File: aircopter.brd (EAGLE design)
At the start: 47 x 28 mm, 44 parts, among them IC1 STF202-22T1G, M1 WIRELESS-NRF24L01, U2 GY-521MPU6050, Y1 20 MHz

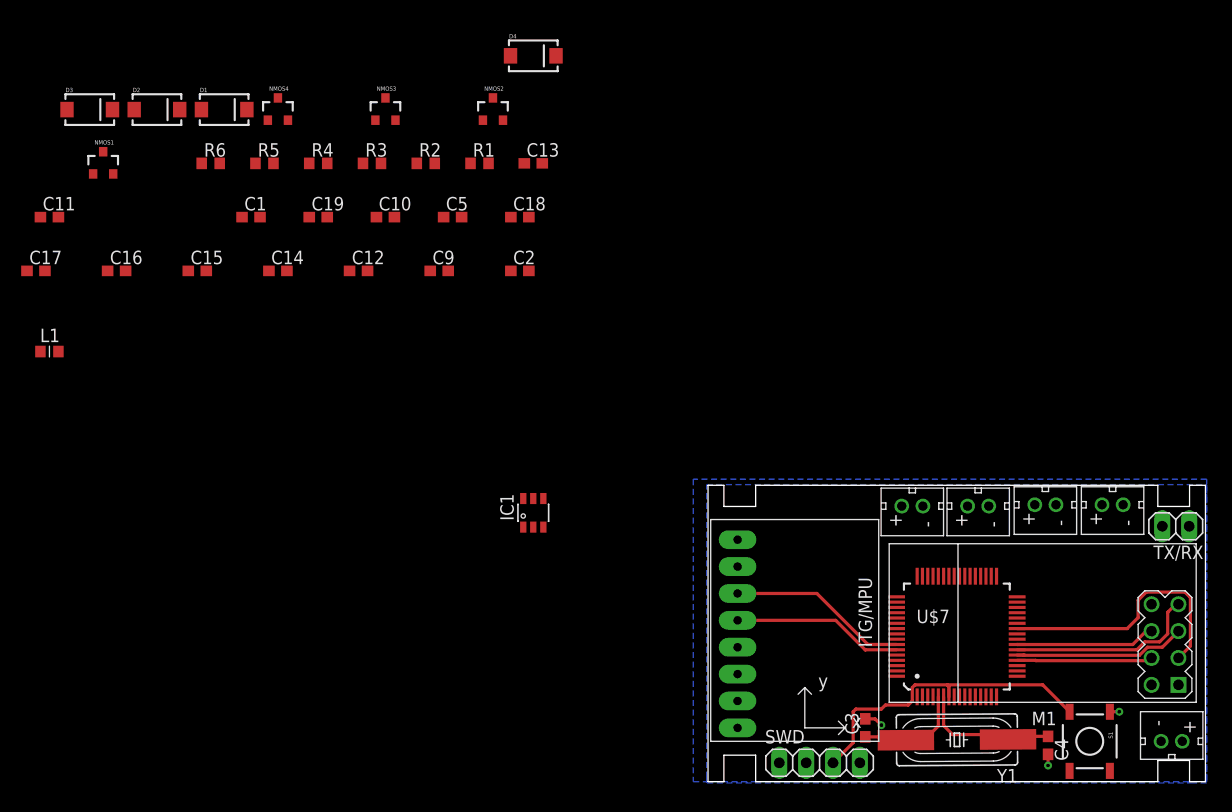
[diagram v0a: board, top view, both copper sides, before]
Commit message: Added Various Decoupling Caps
Can someone check them b4 merge with master pls
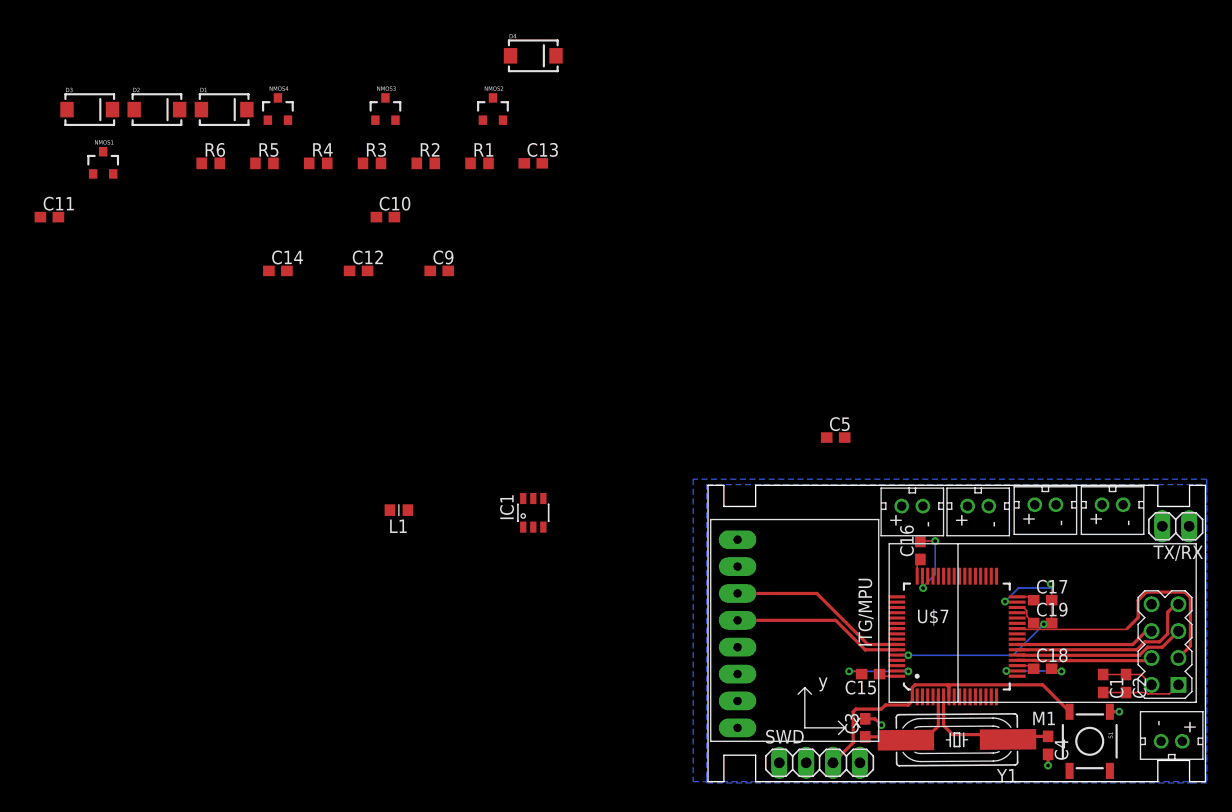
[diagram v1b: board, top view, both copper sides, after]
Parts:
- moved C17 100.1 mm to (31.6, 17.1)
- moved C1 91.8 mm to (37.3, 9.27), turned to 270 degrees
- moved C16 80.4 mm to (20.1, 21.8), turned to 90 degrees
- moved C19 78.5 mm to (31.6, 15.0)
- moved C15 74.2 mm to (15.4, 10.2), turned to 180 degrees
- moved C2 69.3 mm to (39.5, 9.27), turned to 270 degrees
- moved C18 65.3 mm to (31.6, 10.7)
- moved C5 41.8 mm to (12.1, 32.5)
- moved L1 36.3 mm to (-29.2, 25.7), turned to 180 degrees
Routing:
- net GND: track 3.71 -> 60.0 mm, vias 3 -> 13
- net 3V3: track 0.00 -> 11.7 mm
- net N$7: track 0.00 -> 2.47 mm
- net CE: track 25.2 -> 24.6 mm

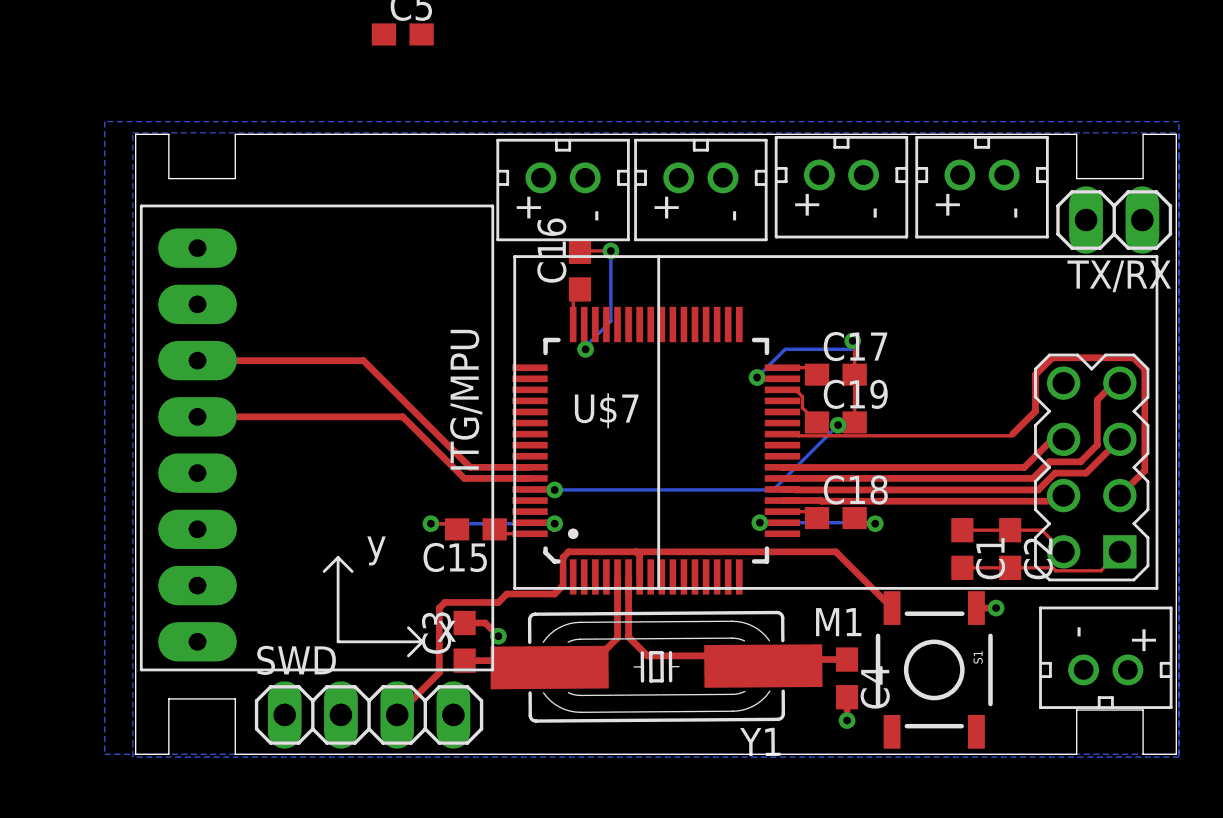
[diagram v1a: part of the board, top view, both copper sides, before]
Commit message: Fixed bugs, removed GND traces
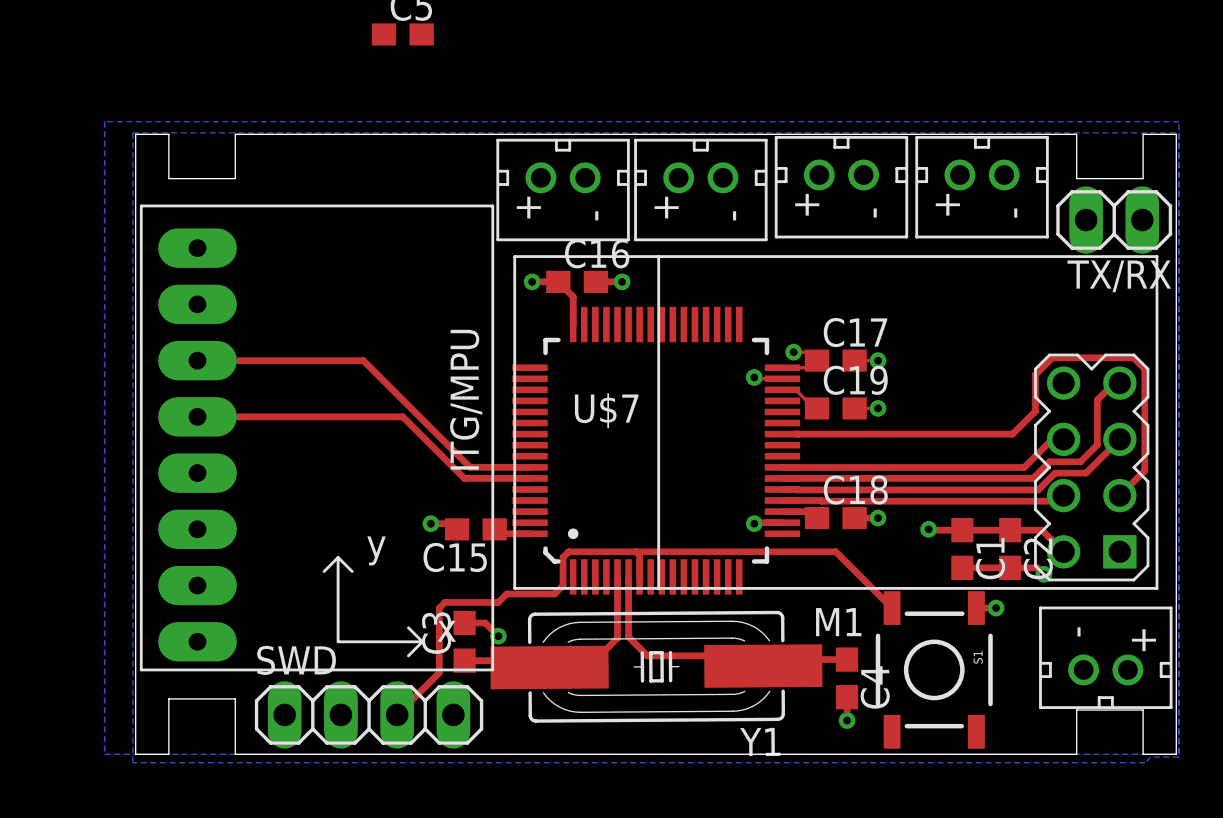
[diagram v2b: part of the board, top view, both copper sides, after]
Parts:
- moved C17 0.64 mm to (31.6, 17.8)
- moved C19 0.63 mm to (31.6, 15.6)
- moved C16 0.52 mm to (19.9, 21.3), turned to 0 degrees
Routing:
- net GND: track 60.0 -> 16.1 mm, vias 13 -> 11
- net 3V3: track 11.7 -> 16.2 mm, vias 0 -> 3
- net N$7: track 2.47 -> 1.91 mm

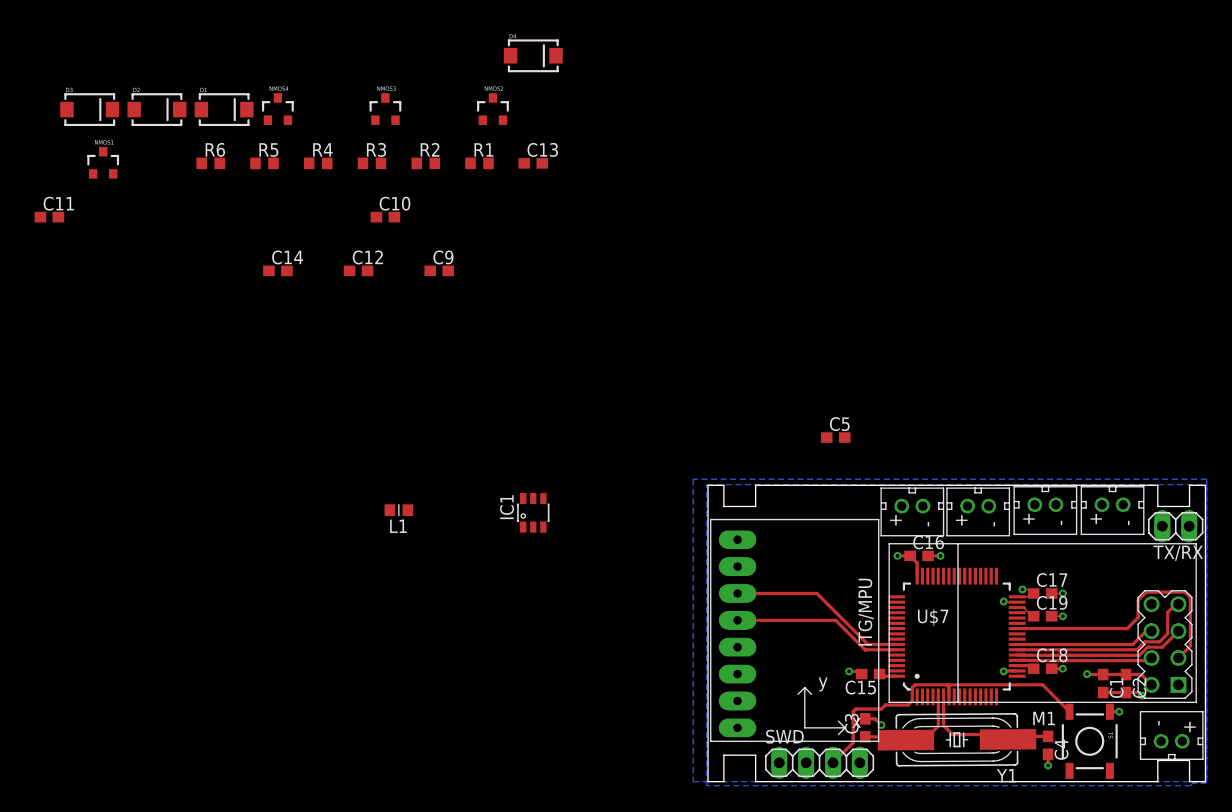
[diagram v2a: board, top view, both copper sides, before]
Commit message: Added remaining caps, organized remaining components
We're still missing the voltage regulator, voltage divider, and motor drivers,
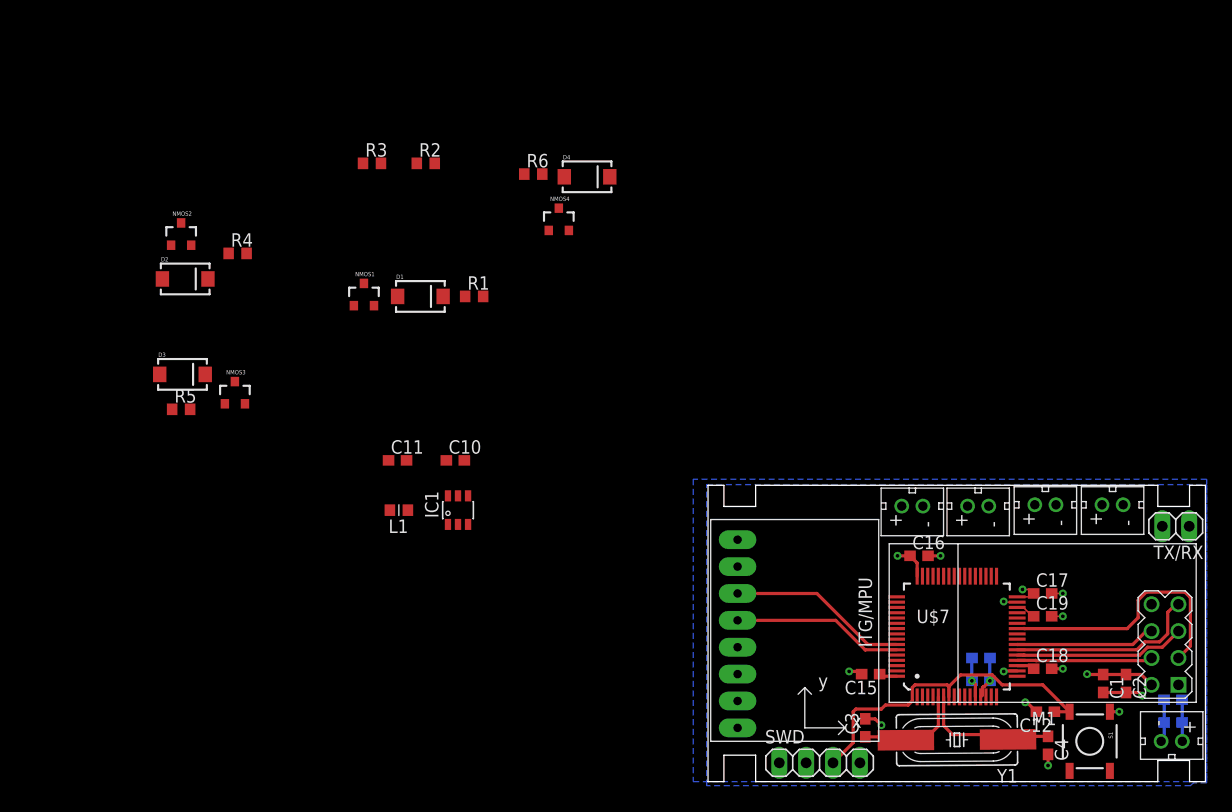
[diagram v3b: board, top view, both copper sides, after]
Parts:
- moved C9 80.3 mm to (43.9, 7.75), flipped to the bottom
- moved C13 80.3 mm to (43.9, 5.59), flipped to the bottom
- moved C12 77.1 mm to (31.9, 6.60), turned to 180 degrees
- moved C14 75.8 mm to (25.8, 11.7), flipped to the bottom
- moved C11 40.1 mm to (-29.3, 30.4)
- moved NMOS2 31.7 mm to (-49.8, 51.7)
- moved R6 30.5 mm to (-16.5, 57.4)
- moved NMOS3 30.3 mm to (-44.7, 36.7)
- moved NMOS4 28.5 mm to (-14.1, 53.1)
- moved NMOS1 27.6 mm to (-32.5, 46.0)
- moved C5 26.8 mm to (25.8, 9.53), flipped to the bottom
- moved D3 26.5 mm to (-49.7, 38.5)
- moved D1 25.6 mm to (-27.2, 45.8)
- moved R5 24.5 mm to (-49.8, 35.2)
- moved C10 23.9 mm to (-23.9, 30.4)
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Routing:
- net GND: track 16.1 -> 25.4 mm, vias 11 -> 13
- net 3V3: track 16.2 -> 20.2 mm, vias 3 -> 4
- net 3V7: track 0.00 -> 3.95 mm
- net RST: track 30.1 -> 32.2 mm

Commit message: Bug Fixes
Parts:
- moved C11 40.1 mm to (-62.2, 53.3)
- moved NMOS4 35.5 mm to (-45.6, 69.5)
- moved R6 30.5 mm to (-47.0, 58.4)
- moved NMOS3 30.3 mm to (-30.5, 63.5)
- moved NMOS1 27.6 mm to (-57.1, 58.4)
- moved D3 26.5 mm to (-58.4, 63.5)
- moved D1 25.6 mm to (-45.7, 63.5)
- moved NMOS2 24.7 mm to (-32.5, 69.3)
- moved R5 24.5 mm to (-41.9, 58.4)
- moved C10 23.9 mm to (-30.5, 53.3)
- moved D2 23.6 mm to (-34.8, 66.0)
- moved R1 12.6 mm to (-21.6, 58.4)
- moved D4 12.5 mm to (-16.5, 68.6)
- moved R4 11.4 mm to (-36.8, 58.4)
- moved IC1 7.12 mm to (-16.5, 25.4)
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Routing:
- net GND: track 25.4 -> 27.7 mm, vias 13 -> 14
- net 3V3: track 20.2 -> 22.1 mm, vias 4 -> 5

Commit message: Reorganized Remaining Comps, various bug fixes
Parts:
- moved C11 58.4 mm to (-13.1, 21.7)
- moved NMOS4 39.5 mm to (-16.9, 42.3)
- moved R1 34.5 mm to (-55.4, 51.3)
- moved D3 32.1 mm to (-30.5, 47.6)
- moved R6 30.7 mm to (-17.0, 51.8)
- moved R3 30.6 mm to (-2.29, 50.0)
- moved C10 30.5 mm to (-12.8, 28.4)
- moved NMOS2 28.7 mm to (-43.4, 42.8)
- moved R2 26.9 mm to (-2.16, 47.2)
- moved D4 21.0 mm to (-16.5, 47.6)
- moved NMOS3 20.7 mm to (-30.6, 42.8)
- moved D2 20.2 mm to (-43.2, 47.6)
- moved D1 18.8 mm to (-55.5, 47.5)
- moved NMOS1 15.6 mm to (-55.4, 42.9)
- moved R5 12.8 mm to (-30.9, 51.9)
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
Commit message: pcb rough draft
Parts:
- moved D1 89.4 mm to (30.1, 21.8), flipped to the bottom, turned to 180 degrees
- moved R1 89.2 mm to (27.4, 18.2), flipped to the bottom
- moved NMOS1 82.6 mm to (24.3, 20.8), flipped to the bottom
- moved D2 82.5 mm to (34.8, 20.6)
- moved NMOS2 76.0 mm to (29.2, 20.4), turned to 270 degrees
- moved R4 75.6 mm to (26.0, 21.3)
- moved R5 54.5 mm to (14.6, 22.0), turned to 180 degrees
- moved D3 50.0 mm to (9.78, 18.0), turned to 180 degrees
- moved NMOS3 48.8 mm to (14.6, 24.5)
- moved R3 46.3 mm to (24.9, 12.6), flipped to the bottom, turned to 270 degrees
- moved R2 45.3 mm to (27.1, 12.6), flipped to the bottom, turned to 90 degrees
- moved R6 39.1 mm to (9.78, 23.4), turned to 180 degrees
- moved L1 33.7 mm to (9.91, 10.5)
- moved D4 32.3 mm to (6.48, 24.9), turned to 270 degrees
- moved NMOS4 31.3 mm to (9.78, 25.9)
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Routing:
- net GND: track 27.7 -> 59.6 mm, vias 14 -> 22
- net RX: track 0.00 -> 30.6 mm, vias 0 -> 1
- net PWM4: track 0.00 -> 26.9 mm
- net TX: track 0.00 -> 26.7 mm, vias 0 -> 1
- net SWDIO: track 0.00 -> 25.0 mm, vias 0 -> 1
- net 3V7: track 3.95 -> 28.1 mm, vias 0 -> 5
- net SWCLK: track 0.00 -> 24.1 mm
- net N$4: track 0.00 -> 20.7 mm
- net 3V3: track 22.1 -> 39.5 mm
- net N$3: track 0.00 -> 17.3 mm
- net N$1: track 0.00 -> 16.1 mm
- net PWM3: track 0.00 -> 14.2 mm
- net N$2: track 0.00 -> 7.89 mm
- net VDIV: track 0.00 -> 6.17 mm, vias 0 -> 1
- net PWM2: track 0.00 -> 4.73 mm
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- added copper zone on layer 16, net 3V7

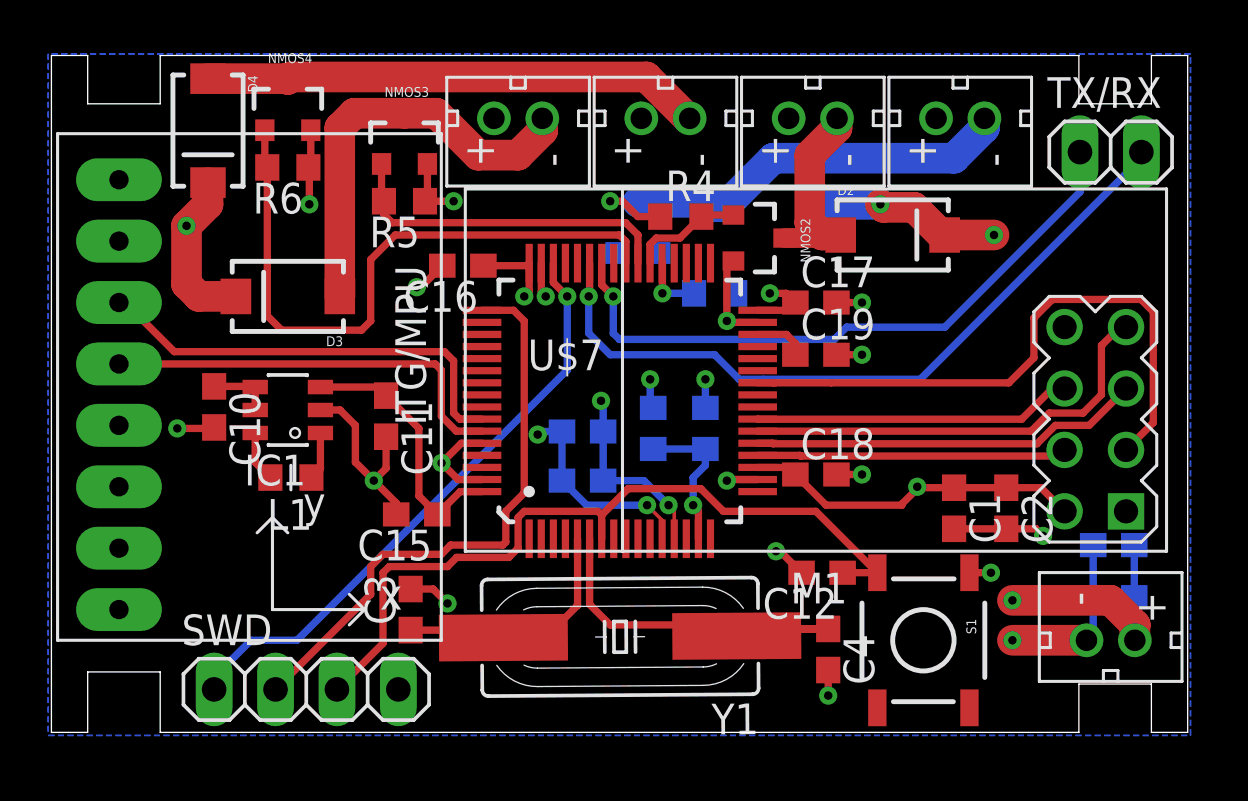
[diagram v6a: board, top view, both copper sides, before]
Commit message: got rid of airwires
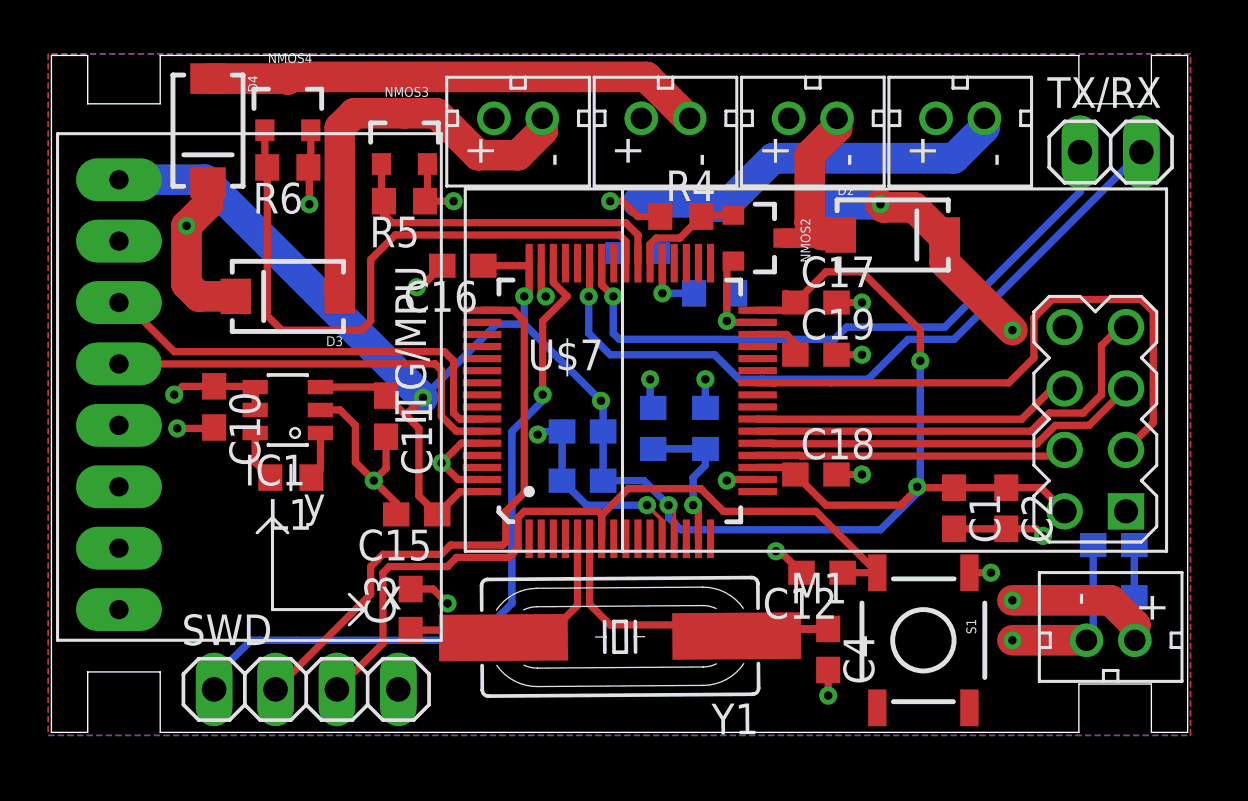
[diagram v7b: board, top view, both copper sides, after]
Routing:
- net 3V3: track 39.5 -> 92.4 mm, vias 5 -> 6
- net 3V7: track 28.1 -> 33.0 mm, vias 5 -> 6
- net SWDIO: track 25.0 -> 29.4 mm
- added copper zone on layer 1, net 3V7
- removed copper zone on layer 16, net 3V7
